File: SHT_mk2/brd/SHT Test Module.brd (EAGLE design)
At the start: 38.1 x 38.2 mm, 12 parts

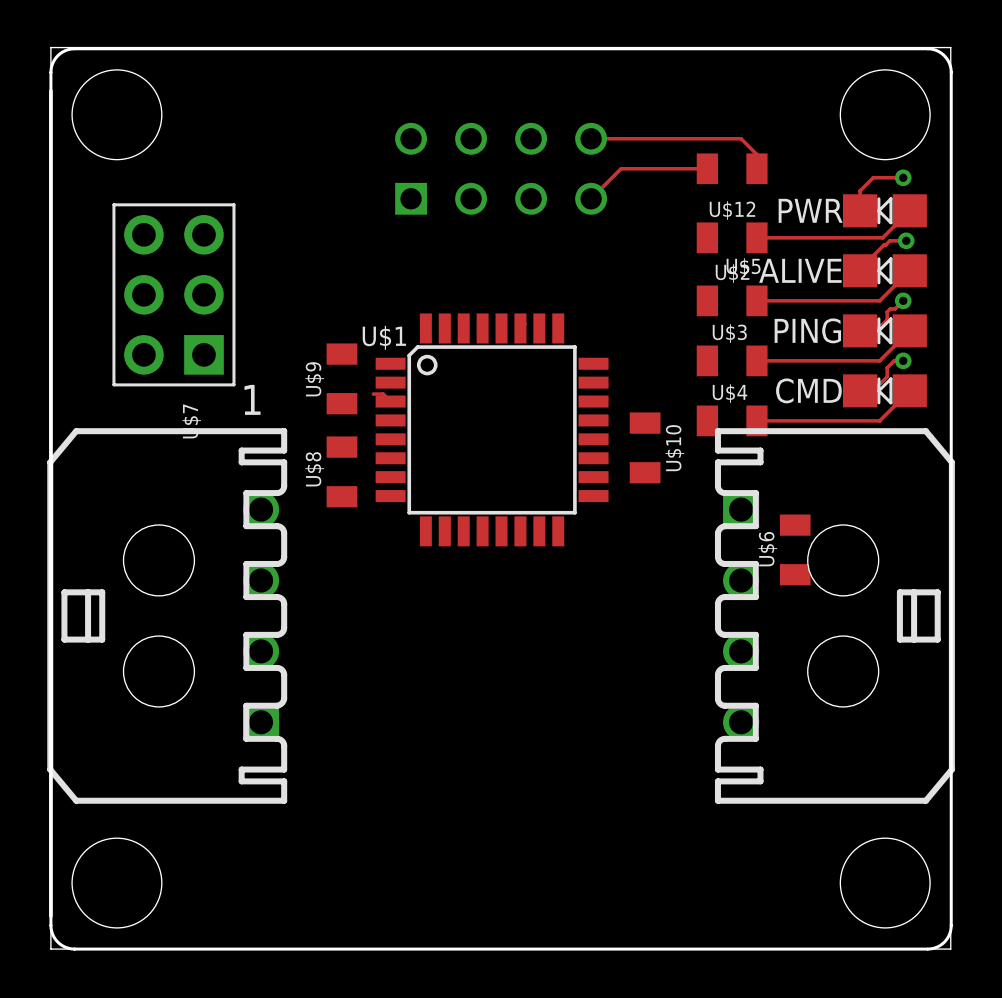
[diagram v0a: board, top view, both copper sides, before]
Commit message: pulled over the SHT mk2 brd files from nathan's branch.
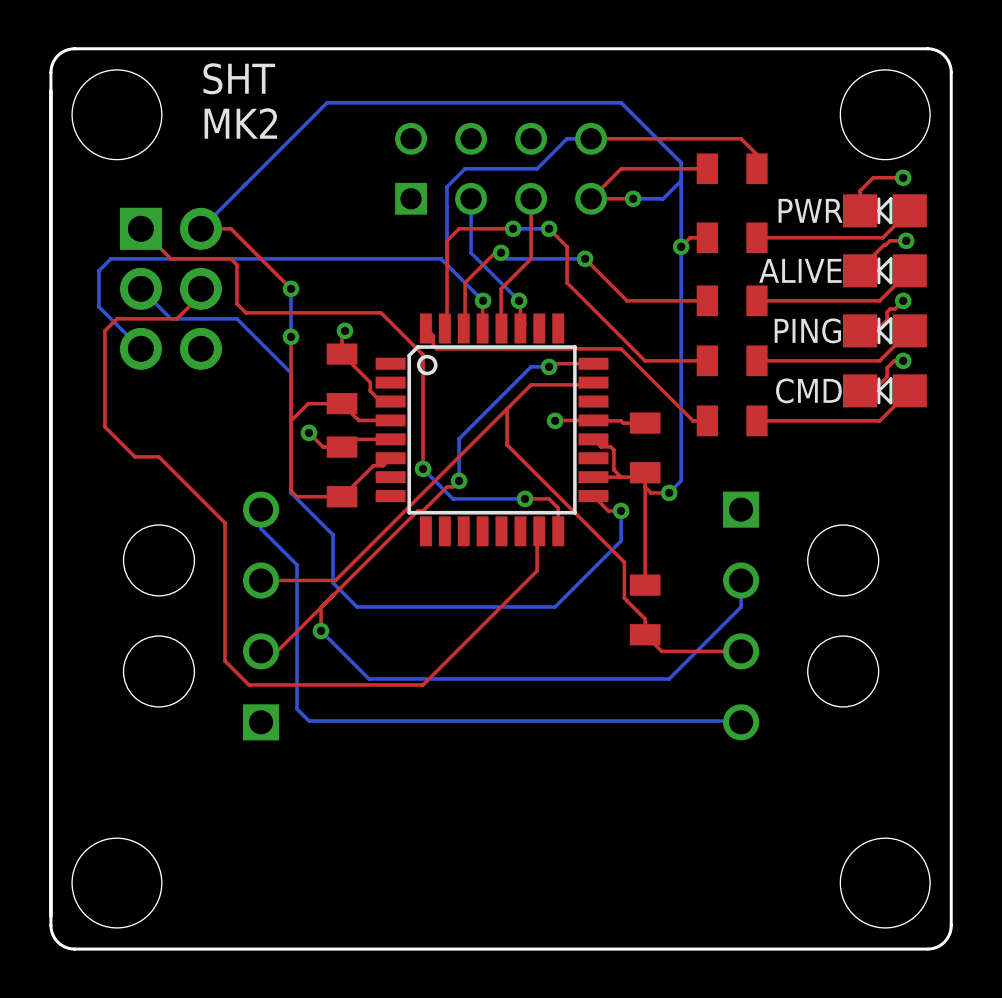
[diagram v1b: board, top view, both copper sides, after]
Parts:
- removed U$7: (no value), 000_CustomPartsMaster:6PINHEADER_CORRECT
- SHT: value SENSOR_MODULE_MK1 -> MK2
- moved U$6 6.84 mm to (25.1, 14.4)
- renumbered TESTMOUDULE to SHT
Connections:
- net GND: now also SHT.GND@4; no longer U$7.6
- net MISO: now also SHT.MISO; no longer U$7.1
- net MOSI: now also SHT.MOSI; no longer U$7.4
- net POWER: now also SHT.3P3V@4; no longer U$7.2
- net RESET: now also SHT.RESET@1, SHT.RESET@2; no longer SHT.RESET, U$7.5
- net SCK: now also SHT.SCK; no longer U$7.3
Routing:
- net POWER: track 5.45 -> 82.4 mm, vias 0 -> 5
- net CLK: track 0.00 -> 42.9 mm, vias 0 -> 3
- net MOSI: track 0.00 -> 39.0 mm
- net DATA: track 0.00 -> 34.1 mm
- net SCK: track 0.00 -> 33.9 mm, vias 0 -> 1
- net RESET: track 7.90 -> 40.6 mm, vias 0 -> 1
- net 3P3V: track 0.00 -> 28.1 mm
- net MISO: track 0.00 -> 27.3 mm, vias 0 -> 2
- net PING: track 0.00 -> 18.2 mm, vias 0 -> 2
- net CMD: track 0.00 -> 13.8 mm
- net ALIVE: track 0.00 -> 13.6 mm, vias 0 -> 2
- net GND: track 11.7 -> 22.7 mm, vias 4 -> 7
- net SDA: track 0.28 -> 6.63 mm, vias 0 -> 1
- net SCL: track 0.00 -> 6.02 mm
- added copper zone on layer 16, net GND
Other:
- board size 38.1 x 38.2 mm -> 38.1 x 38.1 mm
